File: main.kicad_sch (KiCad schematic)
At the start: 124 parts, among them SW1 SW_Push

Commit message: Finalilize the Keybord Shematic
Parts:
- added D? (x14): D, symbol Device:D
- added SW? (x14): SW_Push, JonasLib-Git:MX100H, symbol Switch:SW_Push
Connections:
- net COL0: now also SW?.1
- net COL1: now also SW?.1
- net COL10: now also SW?.1
- net COL11: now also SW?.1
- net COL12: now also SW?.1
- net COL2: now also SW?.1
- net COL3: now also SW?.1
- net COL4: now also SW?.1
- net COL5: now also SW?.1
- net COL6: now also SW?.1
- net COL7: now also SW?.1
- net COL8: now also SW?.1
- net COL9: now also SW?.1
- net ROW2: now also D?.1 (K), D?.1 (K), D?.1 (K), D?.1 (K), D?.1 (K), D?.1 (K), D?.1 (K), D?.1 (K), D?.1 (K), D?.1 (K), D?.1 (K), D?.1 (K), D?.1 (K), D?.1 (K); no longer D?.1 (K), D?.1 (K), D?.1 (K), D?.1 (K), D?.1 (K), D?.1 (K), D?.1 (K), D?.1 (K), D?.1 (K), D?.1 (K), D?.1 (K), D?.1 (K), D?.1 (K)
- net ROW3: now also D?.1 (K), D?.1 (K), D?.1 (K), D?.1 (K), D?.1 (K), D?.1 (K), D?.1 (K), D?.1 (K), D?.1 (K), D?.1 (K), D?.1 (K), D?.1 (K), D?.1 (K); no longer D?.1 (K), D?.1 (K), D?.1 (K), D?.1 (K), D?.1 (K), D?.1 (K), D?.1 (K), D?.1 (K), D?.1 (K), D?.1 (K), D?.1 (K), D?.1 (K)
- net ROW4: now also D?.1 (K), D?.1 (K), D?.1 (K), D?.1 (K), D?.1 (K), D?.1 (K), D?.1 (K), D?.1 (K), D?.1 (K), D?.1 (K), D?.1 (K), D?.1 (K); no longer D?.1 (K), D?.1 (K), D?.1 (K), D?.1 (K), D?.1 (K), D?.1 (K), D?.1 (K), D?.1 (K), D?.1 (K)
- new net: D?.2 (A), SW?.2 (x14)
- new net ROW5: D?.1 (K), D?.1 (K), D?.1 (K), D?.1 (K), D?.1 (K), D?.1 (K), D?.1 (K), D?.1 (K), D?.1 (K)
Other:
- moved on the sheet: D?, SW?

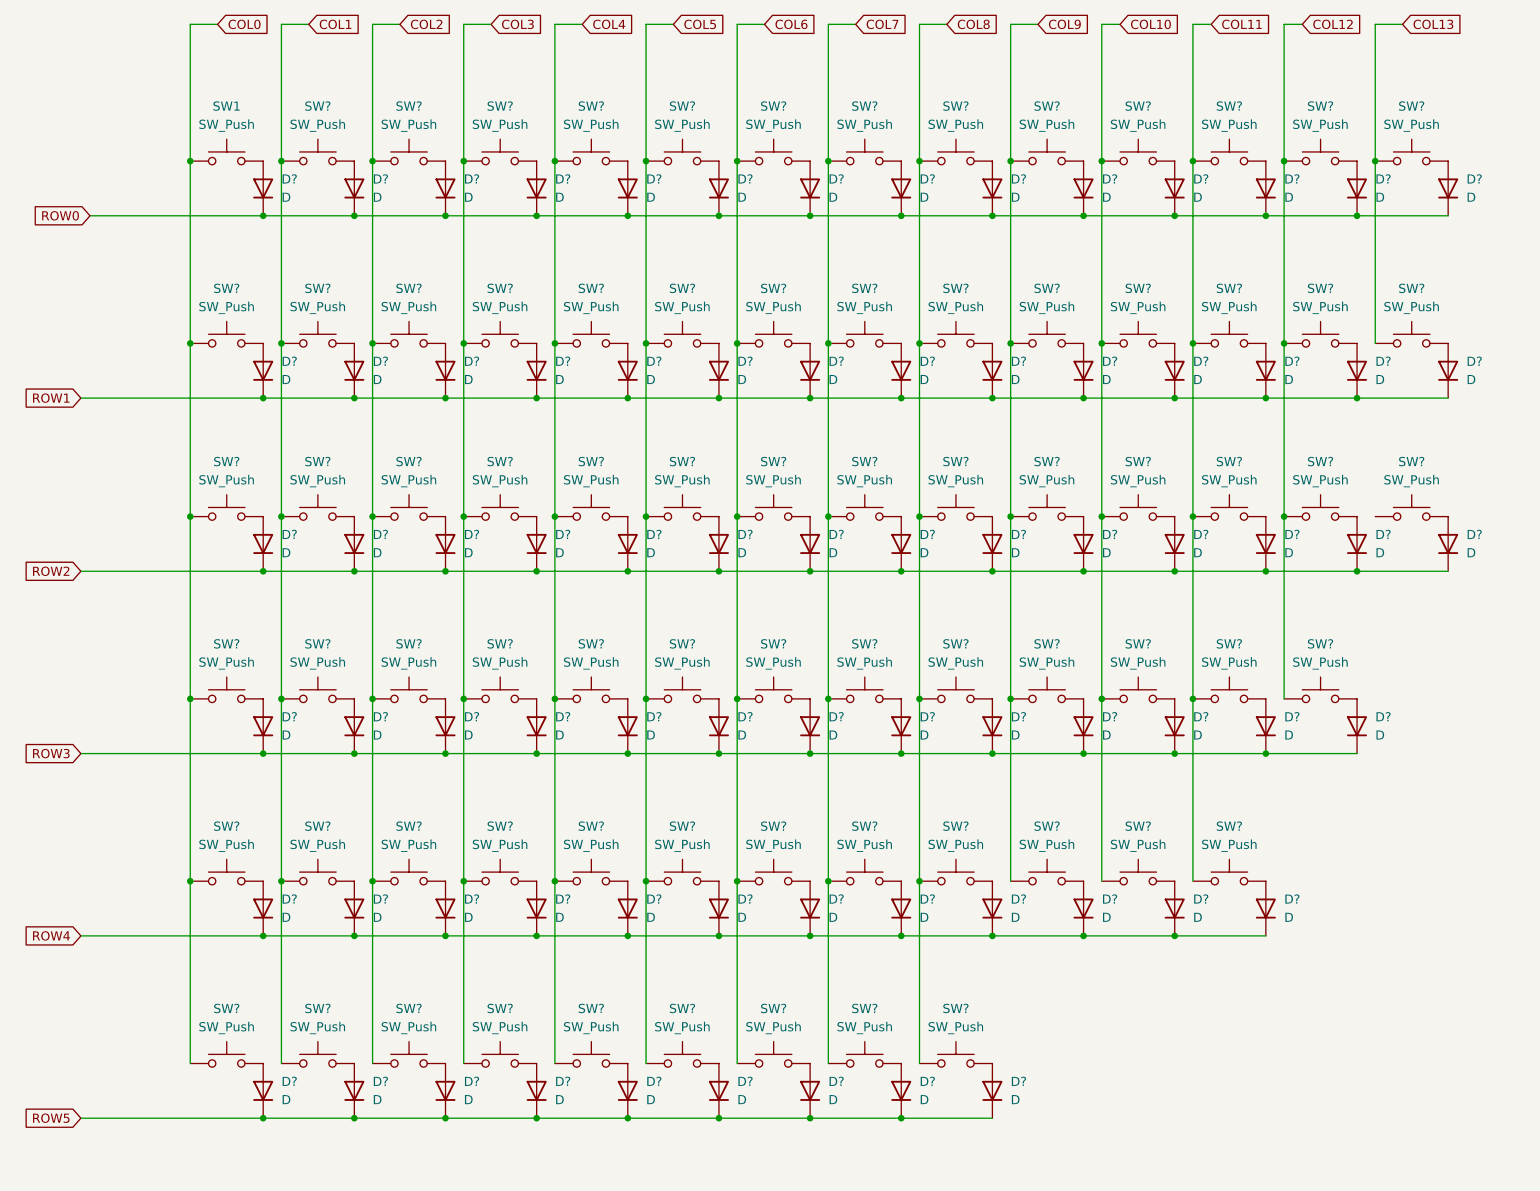
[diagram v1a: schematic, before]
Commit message: Start to fix ERC
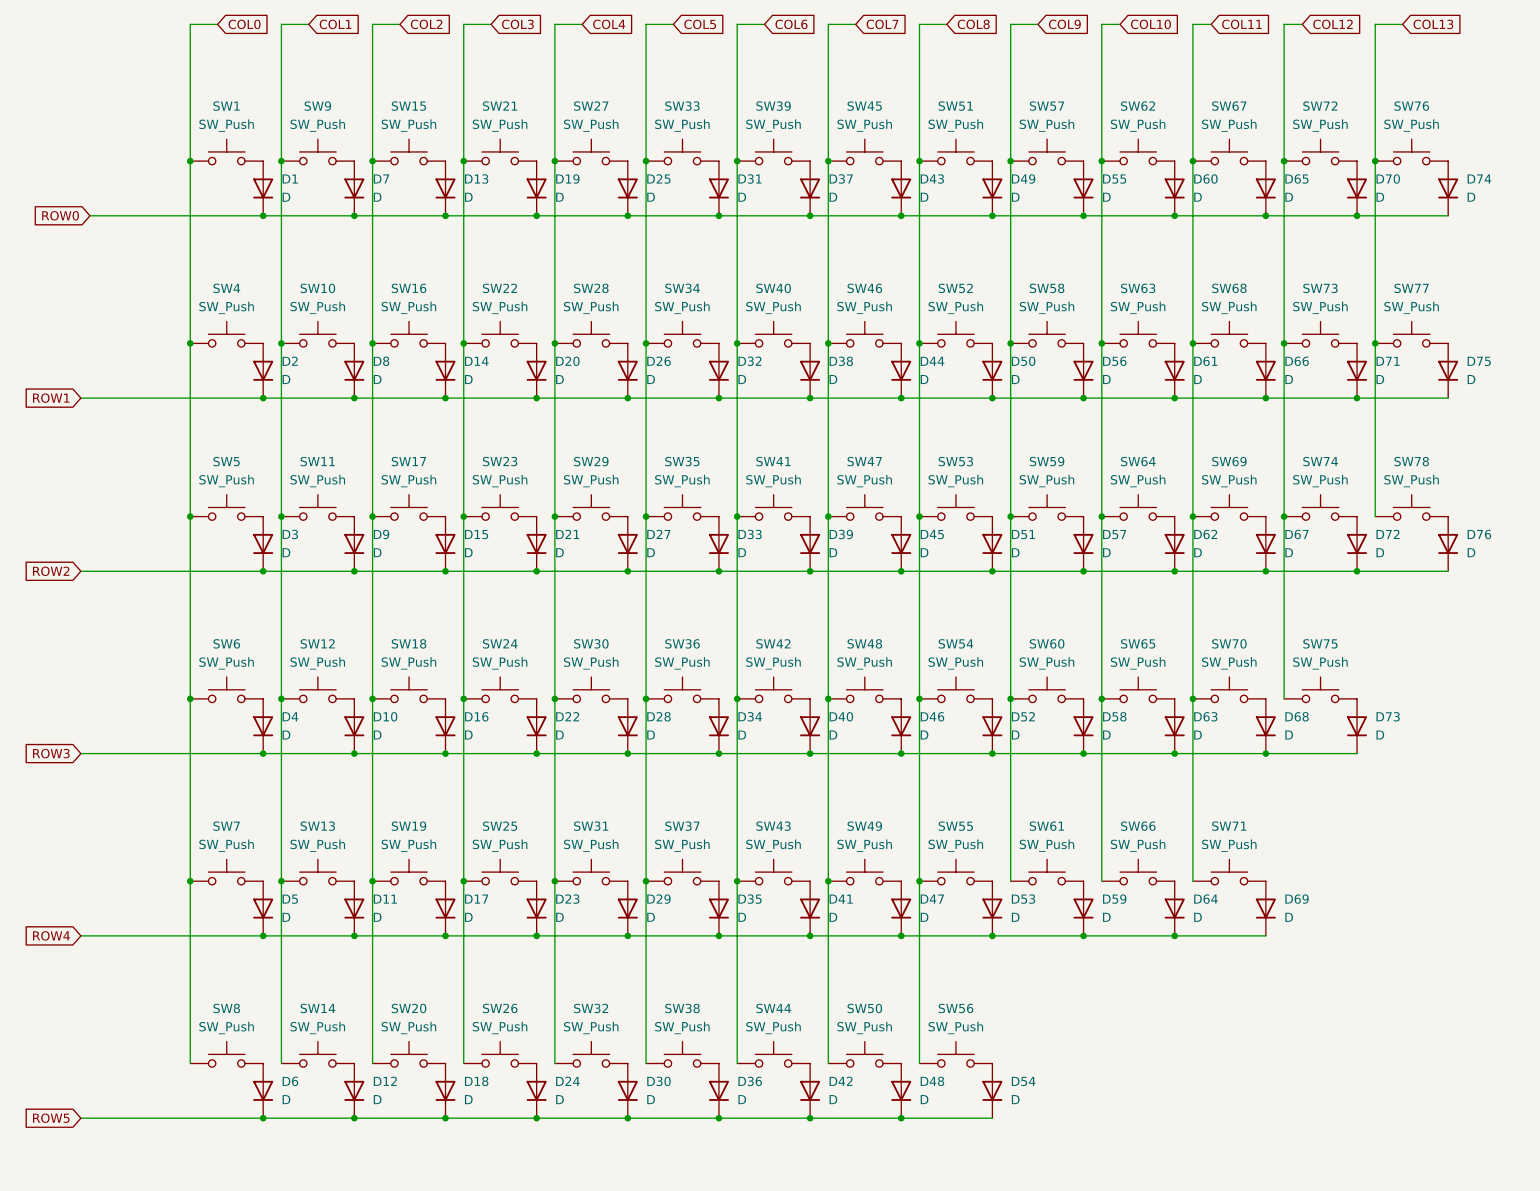
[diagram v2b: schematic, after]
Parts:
- gave numbers to parts that had none: 151
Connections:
- net COL13: now also SW78.1

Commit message: Fixing. Add Footprints
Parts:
- D1, D10, D11, D12, D13, D14, D15, D16, D17, D18, D19, D2, D20, D21, D22, D23, D24, D25, D26, D27, D28, D29, D3, D30, D31, D32, D33, D34, D35, D36, D37, D38, D39, D4, D40, D41, D42, D43, D44, D45, D46, D47, D48, D49, D5, D50, D51, D52, D53, D54, D55, D56, D57, D58, D59, D6, D60, D61, D62, D63, D64, D65, D66, D67, D68, D69, D7, D70, D71, D72, D73, D74, D75, D76, D8, D9: footprint (none) -> Diode_SMD:D_SOD-123

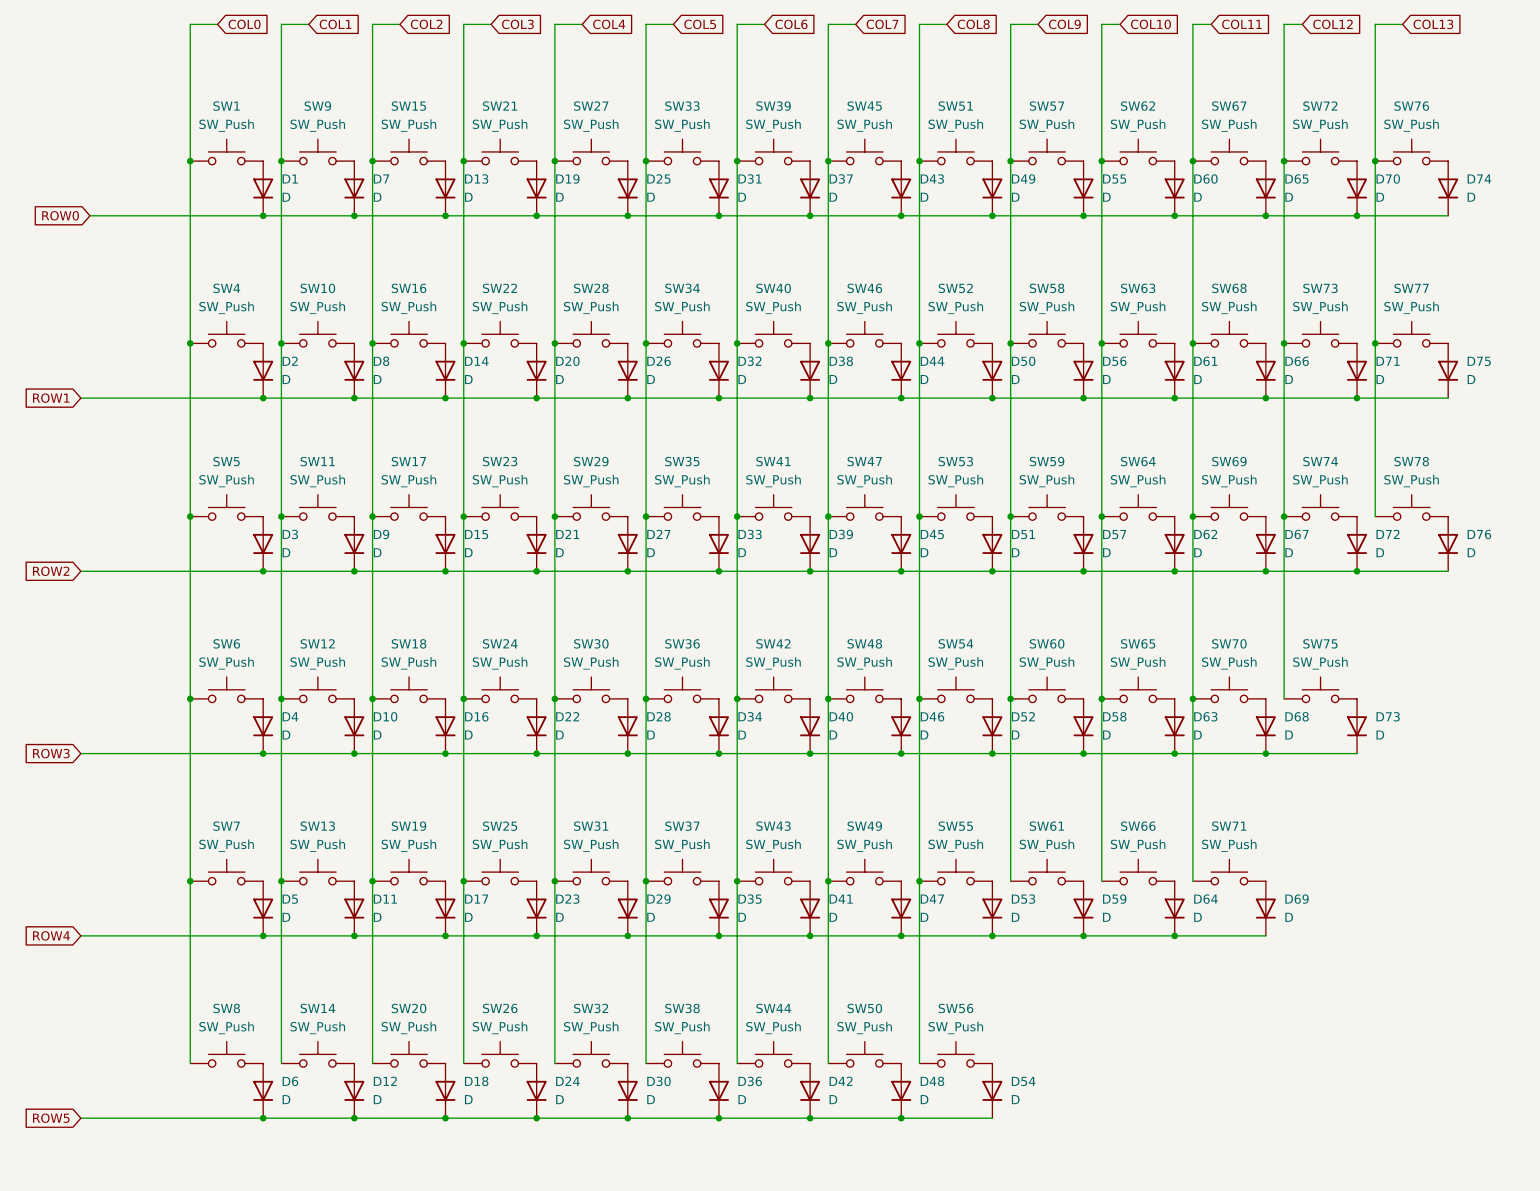
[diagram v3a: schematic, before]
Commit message: Switch Layout on PCB
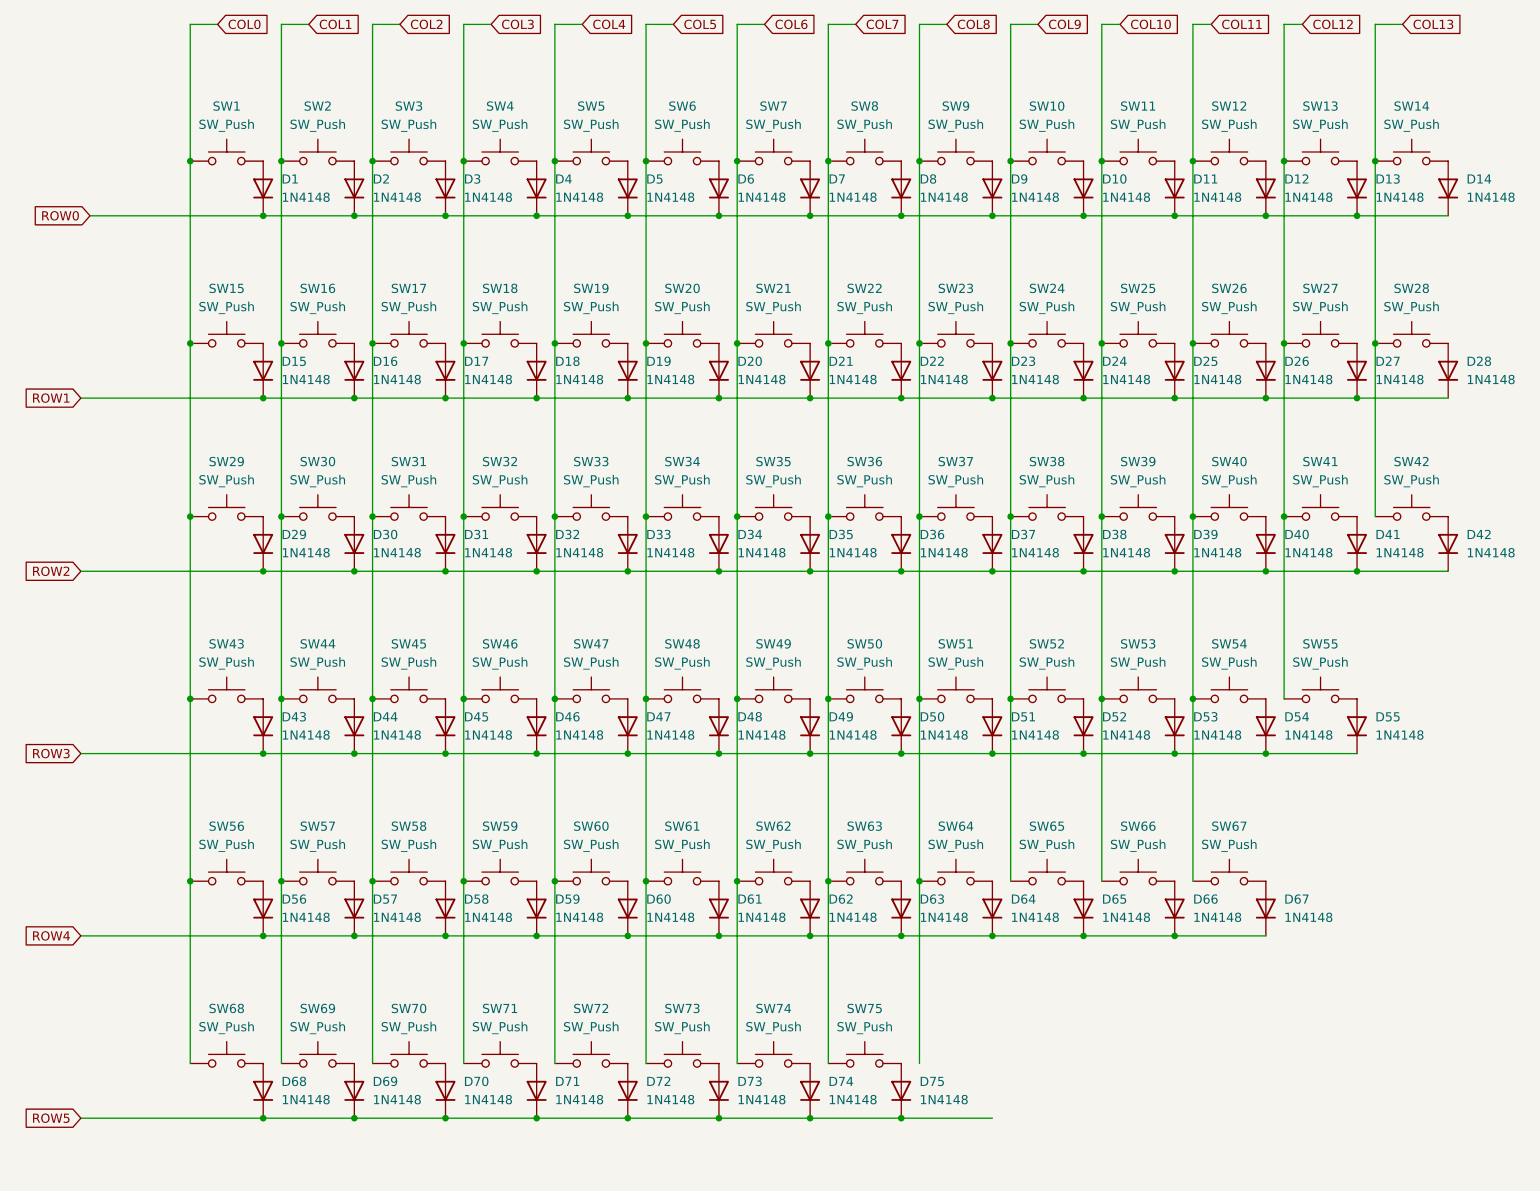
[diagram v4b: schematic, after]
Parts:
- removed D54: D, Diode_SMD:D_SOD-123, symbol Device:D
- removed SW56: SW_Push, JonasLib-Git:MX100H, symbol Switch:SW_Push
- D1: value D -> 1N4148
- D10: renamed from D55; value D -> 1N4148
- D11: renamed from D60; value D -> 1N4148
- D12: renamed from D65; value D -> 1N4148
- D13: renamed from D70; value D -> 1N4148
- D14: renamed from D74; value D -> 1N4148
- D15: renamed from D2; value D -> 1N4148
- D16: renamed from D8; value D -> 1N4148
- D17: renamed from D14; value D -> 1N4148
- D18: renamed from D20; value D -> 1N4148
- D19: renamed from D26; value D -> 1N4148
- D2: renamed from D7; value D -> 1N4148
- D20: renamed from D32; value D -> 1N4148
- D21: renamed from D38; value D -> 1N4148
- D22: renamed from D44; value D -> 1N4148
- D23: renamed from D50; value D -> 1N4148
- D24: renamed from D56; value D -> 1N4148
- D25: renamed from D61; value D -> 1N4148
- D26: renamed from D66; value D -> 1N4148
- D27: renamed from D71; value D -> 1N4148
- D28: renamed from D75; value D -> 1N4148
- D29: renamed from D3; value D -> 1N4148
- D3: renamed from D13; value D -> 1N4148
- D30: renamed from D9; value D -> 1N4148
- D31: renamed from D15; value D -> 1N4148
- D32: renamed from D21; value D -> 1N4148
- D33: renamed from D27; value D -> 1N4148
- D34: renamed from D33; value D -> 1N4148
- D35: renamed from D39; value D -> 1N4148
- D36: renamed from D45; value D -> 1N4148
- D37: renamed from D51; value D -> 1N4148
- D38: renamed from D57; value D -> 1N4148
- D39: renamed from D62; value D -> 1N4148
- D4: renamed from D19; value D -> 1N4148
- D40: renamed from D67; value D -> 1N4148
- D41: renamed from D72; value D -> 1N4148
- D42: renamed from D76; value D -> 1N4148
- D43: renamed from D4; value D -> 1N4148
- D44: renamed from D10; value D -> 1N4148
- D45: renamed from D16; value D -> 1N4148
- D46: renamed from D22; value D -> 1N4148
- D47: renamed from D28; value D -> 1N4148
- D48: renamed from D34; value D -> 1N4148
- D49: renamed from D40; value D -> 1N4148
- D5: renamed from D25; value D -> 1N4148
- D50: renamed from D46; value D -> 1N4148
- D51: renamed from D52; value D -> 1N4148
- D52: renamed from D58; value D -> 1N4148
- D53: renamed from D63; value D -> 1N4148
- D54: renamed from D68; value D -> 1N4148
- D55: renamed from D73; value D -> 1N4148
- D56: renamed from D5; value D -> 1N4148
- D57: renamed from D11; value D -> 1N4148
- D58: renamed from D17; value D -> 1N4148
- D59: renamed from D23; value D -> 1N4148
- D6: renamed from D31; value D -> 1N4148
- D60: renamed from D29; value D -> 1N4148
- D61: renamed from D35; value D -> 1N4148
- D62: renamed from D41; value D -> 1N4148
- D63: renamed from D47; value D -> 1N4148
- D64: renamed from D53; value D -> 1N4148
- D65: renamed from D59; value D -> 1N4148
- D66: renamed from D64; value D -> 1N4148
- D67: renamed from D69; value D -> 1N4148
- D68: renamed from D6; value D -> 1N4148
- D69: renamed from D12; value D -> 1N4148
- D7: renamed from D37; value D -> 1N4148
- D70: renamed from D18; value D -> 1N4148
- D71: renamed from D24; value D -> 1N4148
- D72: renamed from D30; value D -> 1N4148
- D73: renamed from D36; value D -> 1N4148
- D74: renamed from D42; value D -> 1N4148
- D75: renamed from D48; value D -> 1N4148
- D8: renamed from D43; value D -> 1N4148
- D9: renamed from D49; value D -> 1N4148
- renumbered SW57 to SW10, SW62 to SW11, SW67 to SW12, SW72 to SW13, SW76 to SW14, SW4 to SW15, SW10 to SW16, SW16 to SW17, SW22 to SW18, SW28 to SW19, SW9 to SW2, SW34 to SW20, SW40 to SW21, SW46 to SW22, SW52 to SW23, SW58 to SW24, SW63 to SW25, SW68 to SW26, SW73 to SW27, SW77 to SW28, SW5 to SW29, SW15 to SW3, SW11 to SW30, SW17 to SW31, SW23 to SW32, SW29 to SW33, SW35 to SW34, SW41 to SW35, SW47 to SW36, SW53 to SW37, SW59 to SW38, SW64 to SW39, SW21 to SW4, SW69 to SW40, SW74 to SW41, SW78 to SW42, SW6 to SW43, SW12 to SW44, SW18 to SW45, SW24 to SW46, SW30 to SW47, SW36 to SW48, SW42 to SW49, SW27 to SW5, SW48 to SW50, SW54 to SW51, SW60 to SW52, SW65 to SW53, SW70 to SW54, SW75 to SW55, SW7 to SW56, SW13 to SW57, SW19 to SW58, SW25 to SW59, SW33 to SW6, SW31 to SW60, SW37 to SW61, SW43 to SW62, SW49 to SW63, SW55 to SW64, SW61 to SW65, SW71 to SW67, SW8 to SW68, SW14 to SW69, SW39 to SW7, SW20 to SW70, SW26 to SW71, SW32 to SW72, SW38 to SW73, SW44 to SW74, SW50 to SW75, SW45 to SW8, SW51 to SW9
